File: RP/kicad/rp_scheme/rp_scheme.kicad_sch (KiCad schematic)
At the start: 28 parts, among them J1 Screw_Terminal_01x06, J2 Conn_02x03_Odd_Even, K1 Relay_SPST_Latching_2coil, Q1 2N7000, Q2 2N7000, SW1 SW_Push, U1 NRF24L01_Breakout, U2 AMS1117-3.3, U3 STM32F103C6Tx

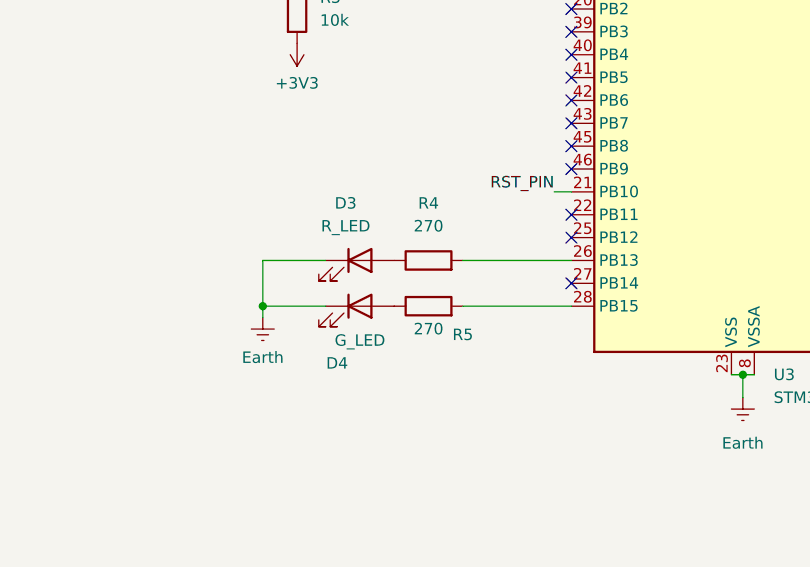
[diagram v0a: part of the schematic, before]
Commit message: РП: изменены габариты платы
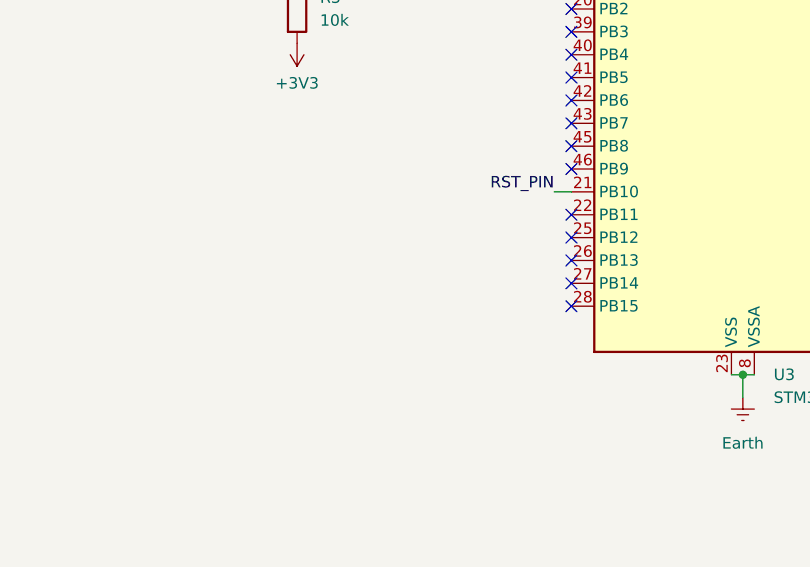
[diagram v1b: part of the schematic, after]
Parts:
- removed D3: R_LED, LED_THT:LED_D3.0mm_Horizontal_O1.27mm_Z2.0mm, symbol Device:LED
- removed D4: G_LED, LED_THT:LED_D3.0mm_Horizontal_O1.27mm_Z2.0mm, symbol Device:LED
- removed R4, R5: 270, Resistor_SMD:R_0603_1608Metric, symbol Device:R
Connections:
- no-connect marks 24 -> 26
